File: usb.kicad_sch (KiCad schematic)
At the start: 24 parts, among them J201 USB_C_Receptacle_USB2.0_16P, J202 Screw_Terminal_01x02, Q1 STL6N3LLH6, U5 TCPP01-M12, U6 USBLC6-2P6, U7 STEF05SGR

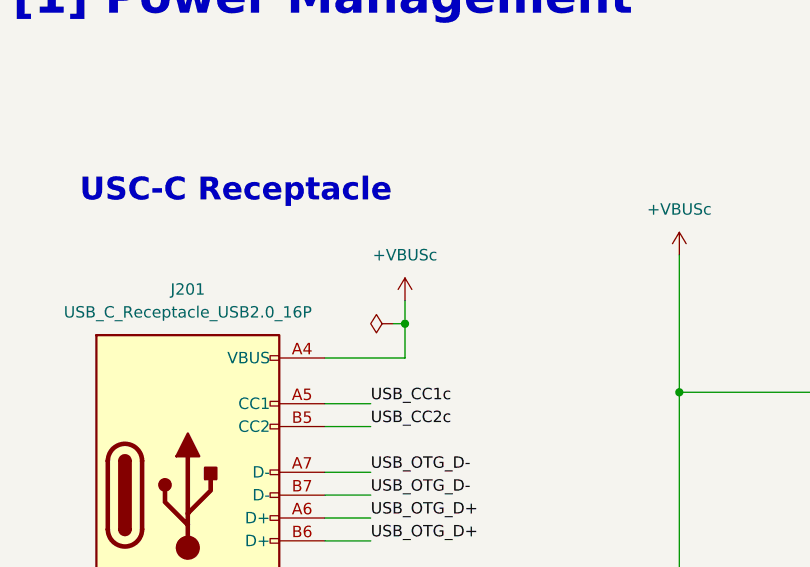
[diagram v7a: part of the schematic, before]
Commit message: schematics errors fixed and ready for PCB
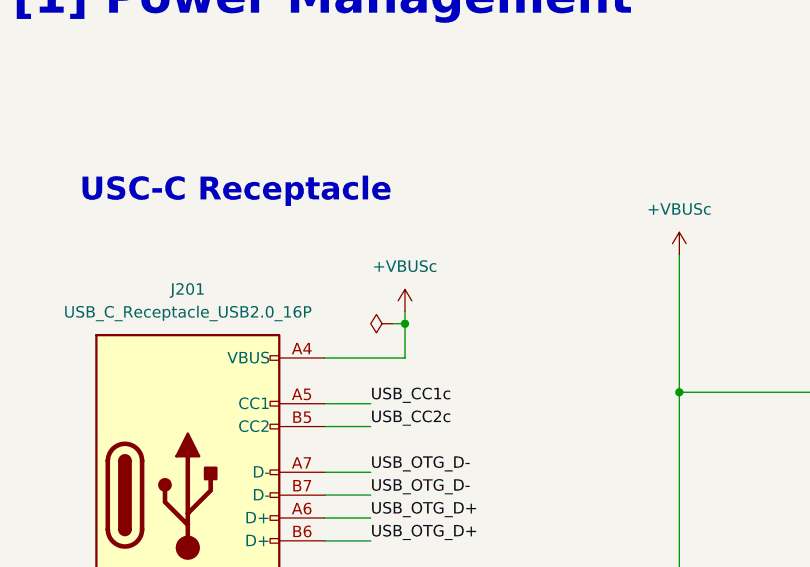
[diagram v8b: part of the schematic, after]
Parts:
- D3: symbol AMS-CM:BAT30KFILM -> EMS:BAT30KFILM
- D4: symbol AMS-CM:ESDA7P60-1U1M -> EMS:ESDA7P60-1U1M
- Q1: symbol AMS-CM:STL6N3LLH6 -> EMS:STL6N3LLH6
- TP4, TP5: Distributor_Link https://www.mouser.com/ProductDetail/Keystone-Electronics/5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 -> (none); Manufacturer_Name Keystone Electronics -> (none); Manufacturer_Part_Number 5000 -> (none)
- U5: symbol AMS-CM:TCPP01-M12 -> EMS:TCPP01-M12
- U6: symbol AMS-CM:USBLC6-2P6 -> EMS:USBLC6-2P6
- U7: symbol AMS-CM:STEF05SGR -> EMS:STEF05SGR
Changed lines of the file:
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@@
 	(wire
 		(pts
-			(xy 57.15 55.88) (xy 57.15 53.34)
+			(xy 57.15 55.88) (xy 57.15 54.61)
 		)
 		(stroke
@@
 	)
 	(symbol
-		(lib_id "AMS-CM:+V_USB")
+		(lib_id "EMS:+V_USB")
 		(at 278.13 97.79 0)
 		(unit 1)
@@
 	)
 	(symbol
-		(lib_id "AMS-CM:+5V_EXT")
+		(lib_id "EMS:+5V_EXT")
 		(at 256.54 97.79 0)
 		(unit 1)
@@
 	)
 	(symbol
-		(lib_id "AMS-CM:ESDA7P60-1U1M")
+		(lib_id "EMS:ESDA7P60-1U1M")
 		(at 76.2 102.87 270)
 		(unit 1)
@@
 	)
 	(symbol
-		(lib_id "AMS-CM:BAT30KFILM")
+		(lib_id "EMS:BAT30KFILM")
 		(at 105.41 99.06 180)
 		(unit 1)
@@
 	)
 	(symbol
-		(lib_id "AMS-CM:+V_USB")
+		(lib_id "EMS:+V_USB")
 		(at 31.75 182.88 0)
 		(unit 1)
@@
 	)
 	(symbol
-		(lib_id "AMS-CM:+VBUSc")
+		(lib_id "EMS:+VBUSc")
 		(at 87.63 48.26 0)
 		(unit 1)
@@
 	)
 	(symbol
-		(lib_id "AMS-CM:STL6N3LLH6")
+		(lib_id "EMS:STL6N3LLH6")
 		(at 138.43 69.85 0)
 		(unit 1)
@@
 	)
 	(symbol
-		(lib_id "AMS-CM:USBLC6-2P6")
+		(lib_id "EMS:USBLC6-2P6")
 		(at 232.41 55.88 0)
 		(unit 1)
@@
 			)
 		)
-		(property "Datasheet" "https://www.mouser.com/datasheet/2/215/000-5004-741320.pdf"
+		(property "Datasheet" "~"
 			(at 52.07 185.42 0)
 			(effects
@@
 			)
 		)
-		(property "Distributor_Link" "https://www.mouser.com/ProductDetail/Keystone-Electronics/5000?qs=q0tsjPZWdm%252B9SiiTAbEwUw%3D%3D"
+		(property "Distributor_Link" "~"
 			(at 52.07 190.5 0)
 			(effects
@@
 			)
 		)
-		(property "Manufacturer_Name" "Keystone Electronics"
+		(property "Manufacturer_Name" "~"
 			(at 52.07 190.5 0)
 			(effects
@@
 			)
 		)
-		(property "Manufacturer_Part_Number" "5000"
+		(property "Manufacturer_Part_Number" "~"
 			(at 52.07 190.5 0)
 			(effects
@@
 	)
 	(symbol
-		(lib_id "AMS-CM:+5V_EXT")
+		(lib_id "EMS:+VBUSc")
+		(at 57.15 54.61 0)
+		(unit 1)
+		(exclude_from_sim no)
+		(in_bom no)
+		(on_board no)
+		(dnp no)
+		(fields_autoplaced yes)
+		(property "Reference" "#PWR0204"
+			(at 61.976 53.086 0)
+			(effects
+				(font
+					(size 1.27 1.27)
+				)
+				(hide yes)
+			)
+		)
+		(property "Value" "+VBUSc"
+			(at 57.15 49.53 0)
+			(effects
+				(font
+					(size 1.27 1.27)
+				)
+			)
+		)
+		(property "Footprint" ""
+			(at 57.15 54.61 0)
+			(effects
+				(font
+					(size 1.27 1.27)
+				)
+				(hide yes)
+			)
+		)
+		(property "Datasheet" ""
+			(at 57.15 54.61 0)
+			(effects
+				(font
+					(size 1.27 1.27)
+				)
+				(hide yes)
+			)
+		)
+		(property "Description" "Power symbol for \"+VBUSc\""
+			(at 58.42 60.452 0)
+			(effects
+				(font
+					(size 1.27 1.27)
+				)
+				(hide yes)
+			)
+		)
+		(pin "1"
+		)
+		(instances
+			(project ""
+				(path "/e660428c-c9b7-476c-8ac8-2d419f233469/7dd15615-8075-471d-b8bf-599b8660331d"
+					(reference "#PWR0204")
+					(unit 1)
+				)
+			)
+		)
+	)
+	(symbol
+		(lib_id "EMS:+5V_EXT")
 		(at 228.6 153.67 0)
 		(unit 1)
@@
 			)
 		)
-		(property "Datasheet" "https://www.mouser.com/datasheet/2/215/000-5004-741320.pdf"
+		(property "Datasheet" "~"
 			(at 24.13 185.42 0)
 			(effects
@@
 			)
 		)
-		(property "Distributor_Link" "https://www.mouser.com/ProductDetail/Keystone-Electronics/5000?qs=q0tsjPZWdm%252B9SiiTAbEwUw%3D%3D"
+		(property "Distributor_Link" "~"
 			(at 24.13 190.5 0)
 			(effects
@@
 			)
 		)
-		(property "Manufacturer_Name" "Keystone Electronics"
+		(property "Manufacturer_Name" "~"
 			(at 24.13 190.5 0)
 			(effects
@@
 			)
 		)
-		(property "Manufacturer_Part_Number" "5000"
+		(property "Manufacturer_Part_Number" "~"
 			(at 24.13 190.5 0)
 			(effects
@@
 	)
 	(symbol
-		(lib_id "AMS-CM:STEF05SGR")
+		(lib_id "EMS:STEF05SGR")
 		(at 228.6 107.95 0)
 		(unit 1)
@@
 	)
 	(symbol
-		(lib_id "AMS-CM:TCPP01-M12")
+		(lib_id "EMS:TCPP01-M12")
 		(at 138.43 114.3 0)
 		(unit 1)
@@
 	)
 	(symbol
-		(lib_id "AMS-CM:+V_USB")
+		(lib_id "EMS:+V_USB")
 		(at 173.99 48.26 0)
 		(unit 1)
@@
 					(unit 1)
 				)
-			)
-		)
-	)
-	(symbol
-		(lib_id "AMS-CM:+VBUSc")
-		(at 57.15 53.34 0)
-		(unit 1)
-		(exclude_from_sim no)
-		(in_bom no)
-		(on_board no)
-		(dnp no)
-		(fields_autoplaced yes)
-		(property "Reference" "#PWR040"
-			(at 57.15 53.34 0)
-			(effects
-				(font
-					(size 1.27 1.27)
-				)
-				(hide yes)
-			)
-		)
-		(property "Value" "+VBUSc"
-			(at 57.15 48.26 0)
-			(effects
-				(font
-					(size 1.27 1.27)
-				)
-			)
-		)
-		(property "Footprint" ""
-			(at 57.15 53.34 0)
-			(effects
-				(font
-					(size 1.27 1.27)
-				)
-				(hide yes)
-			)
-		)
-		(property "Datasheet" ""
-			(at 57.15 53.34 0)
-			(effects
-				(font
-					(size 1.27 1.27)
-				)
-				(hide yes)
-			)
-		)
-		(property "Description" "Power symbol for \"+VBUSc\""
-			(at 58.42 59.182 0)
-			(effects
-				(font
-					(size 1.27 1.27)
-				)
-				(hide yes)
-			)
-		)
-		(pin "1"
-		)
-		(instances
-			(project ""
-				(path "/25e778da-5dc5-4758-a36a-bcdc19e01b9c/8807acf4-e2de-42c2-8667-46d1df70aab4"
-					(reference "#PWR040")
-					(unit 1)
-				)
-			)
-			(project ""
-				(path "/e660428c-c9b7-476c-8ac8-2d419f233469/7dd15615-8075-471d-b8bf-599b8660331d"
-					(reference "#PWR0204")
-					(unit 1)
-				)
